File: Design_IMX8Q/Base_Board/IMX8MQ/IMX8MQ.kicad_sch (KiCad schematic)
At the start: 25 parts, among them U1 MIMX8MQ6CVAHZAB, U2 IS43LQ32256A-062BLI, U6 SDINBDG4-8G, U7 MT25QUxxxxxx1xW7, X1 ABLNO, Y1 25MHz, Y2 27MHz

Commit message: Adding color on LPDDR4 memory net
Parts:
- removed C19, C20, C21, C22: 10pF, Capacitor_SMD:C_0402_1005Metric, symbol Device:C_Small
- removed C23, C24, C25, C26, C28, C29, C67, C68: 0.1uF, Capacitor_SMD:C_0402_1005Metric, symbol Device:C_Small
- removed C27, C30: 4.7F, Capacitor_SMD:C_0402_1005Metric, symbol Device:C_Small
- removed R1: 240 1%, Resistor_SMD:R_0201_0603Metric, symbol Device:R_Small
- removed R10, R9: 1M, Resistor_SMD:R_0402_1005Metric, symbol Device:R_Small
- removed R2: 240, Resistor_SMD:R_0402_1005Metric, symbol Device:R_Small
- removed U1: MIMX8MQ6CVAHZAB, IMX8MQ_footprints:MIMX8MQ6CVAHZAB, symbol _MIMX8MQ6CVAHZAB:MIMX8MQ6CVAHZAB
- removed U2: IS43LQ32256A-062BLI, Package_BGA:BGA-200_10.0x14.5mm_Layout12x22_P0.80x0.65mm, symbol Memory_RAM:IS43LQ32256A-062BLI
- removed U6: SDINBDG4-8G, _W_SBC:BGA153C50P14X14_1300X1150X80N, symbol SDINBDG4-8G:SDINBDG4-8G
- removed U7: MT25QUxxxxxx1xW7, Package_DFN_QFN:W-PDFN-8-1EP_6x5mm_P1.27mm_EP3x3mm, symbol Memory_Flash:MT25QUxxxxxx1xW7
- removed X1: ABLNO, Oscillator:Oscillator_SMD_EuroQuartz_XO32-4Pin_3.2x2.5mm_HandSoldering, symbol Oscillator:ABLNO
- removed Y1: 25MHz, Crystal:Crystal_SMD_3225-4Pin_3.2x2.5mm, symbol Device:Crystal_GND24_Small
- removed Y2: 27MHz, Crystal:Crystal_SMD_3225-4Pin_3.2x2.5mm, symbol Device:Crystal_GND24_Small
- added J1: Bus_PCI_Express_x16, Connector_PCBEdge:BUS_PCIexpress_x16, symbol Connector:Bus_PCI_Express_x16
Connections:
- new net: J1.A10 (+3.3V), J1.A9 (+3.3V), J1.B8 (+3.3V)
- new net: J1.A12 (GND), J1.A15 (GND), J1.A18 (GND), J1.A20 (GND), J1.A23 (GND), J1.A24 (GND), J1.A27 (GND), J1.A28 (GND), J1.A31 (GND), J1.A34 (GND), J1.A37 (GND), J1.A38 (GND), J1.A4 (GND), J1.A41 (GND), J1.A42 (GND), J1.A45 (GND), J1.A46 (GND), J1.A49 (GND), J1.A51 (GND), J1.A54 (GND), J1.A55 (GND), J1.A58 (GND), J1.A59 (GND), J1.A62 (GND), J1.A63 (GND), J1.A66 (GND), J1.A67 (GND), J1.A70 (GND), J1.A71 (GND), J1.A74 (GND), J1.A75 (GND), J1.A78 (GND), J1.A79 (GND), J1.A82 (GND), J1.B13 (GND), J1.B16 (GND), J1.B18 (GND), J1.B21 (GND), J1.B22 (GND), J1.B25 (GND), J1.B26 (GND), J1.B29 (GND), J1.B32 (GND), J1.B35 (GND), J1.B36 (GND), J1.B39 (GND), J1.B4 (GND), J1.B40 (GND), J1.B43 (GND), J1.B44 (GND), J1.B47 (GND), J1.B49 (GND), J1.B52 (GND), J1.B53 (GND), J1.B56 (GND), J1.B57 (GND), J1.B60 (GND), J1.B61 (GND), J1.B64 (GND), J1.B65 (GND), J1.B68 (GND), J1.B69 (GND), J1.B7 (GND), J1.B72 (GND), J1.B73 (GND), J1.B76 (GND), J1.B77 (GND), J1.B80 (GND)
- new net: J1.A2 (+12V), J1.A3 (+12V), J1.B1 (+12V), J1.B2 (+12V), J1.B3 (+12V)
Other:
- sheet System Power renamed GND
- added sheet Clock (Clock.kicad_sch)
- added sheet GPIO I2C MIPI ENET HDMI JTAG (GPIO_I2C_MIPI_ENET_HDMI_JTAG.kicad_sch)
- added sheet LPDDR4 (LPDDR4.kicad_sch)
- added sheet NAND MIPI PCIE (NAND_MIPI_PCIE.kicad_sch)
- added sheet Power_IMX8 (Power_IMX8.kicad_sch)
- added sheet SAI SD SPDIF USB UART (SAI-SD-SPDIF-USB-UART.kicad_sch)
- added sheet VDD (PowerSystem.kicad_sch)

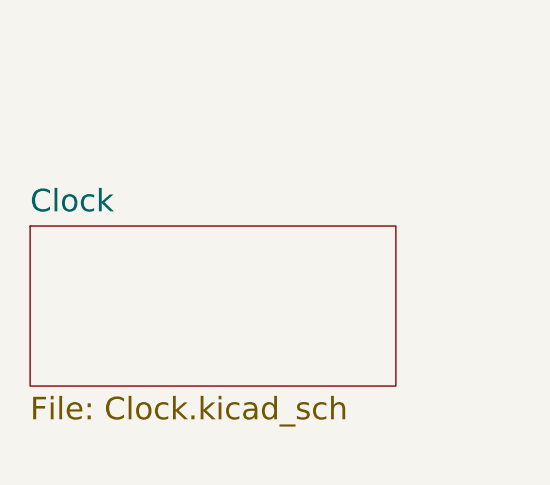
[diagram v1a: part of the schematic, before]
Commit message: changes vias pad size
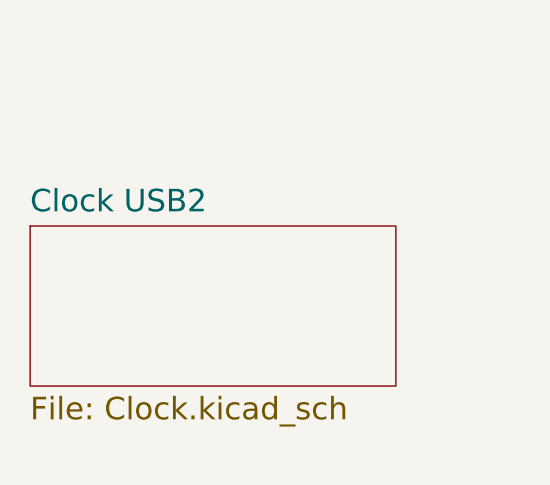
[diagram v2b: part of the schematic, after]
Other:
- sheet Clock renamed Clock USB2
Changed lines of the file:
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@@
     (stroke (width 0.1524) (type solid))
     (fill (color 0 0 0 0.0000))
-    (property "Sheetname" "Clock" (at 31.75 38.0434 0)
+    (property "Sheetname" "Clock USB2" (at 31.75 38.0434 0)
       (effects (font (size 2.5 2.5)) (justify left bottom))
     )

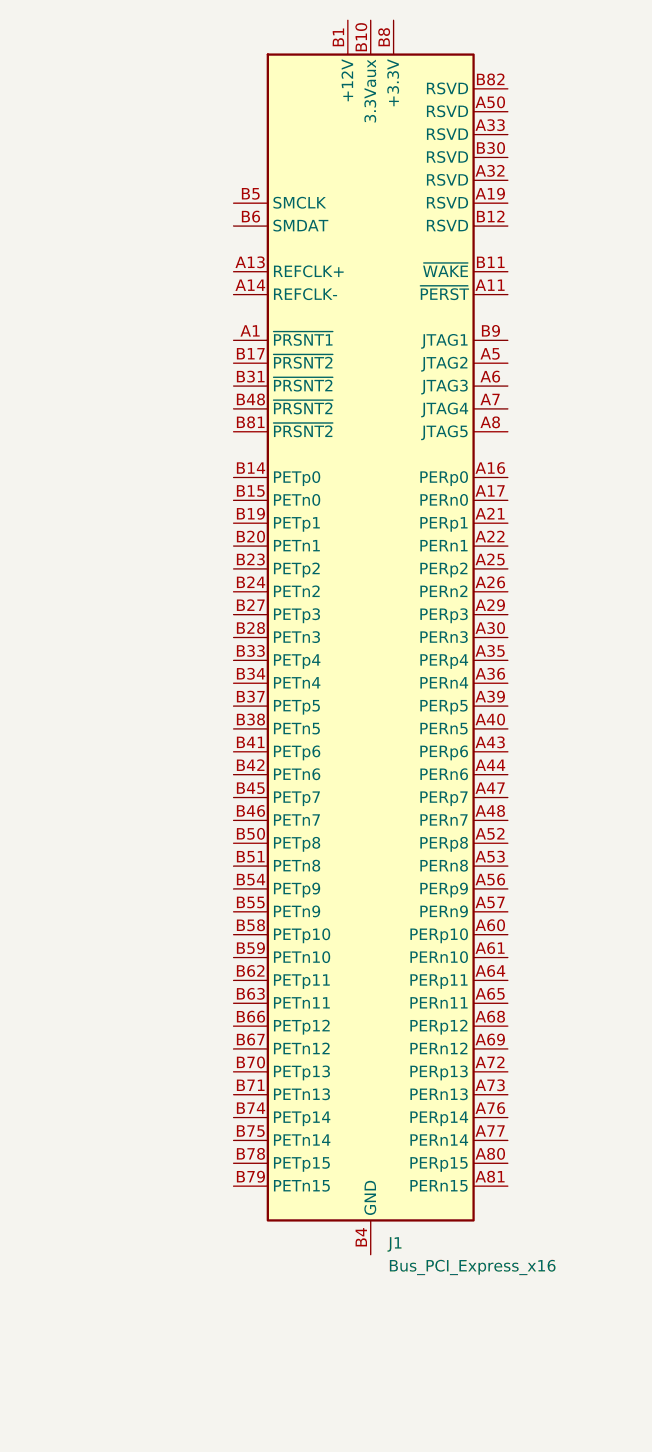
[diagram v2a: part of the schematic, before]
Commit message: Update IMX6QP and IMX8MQ
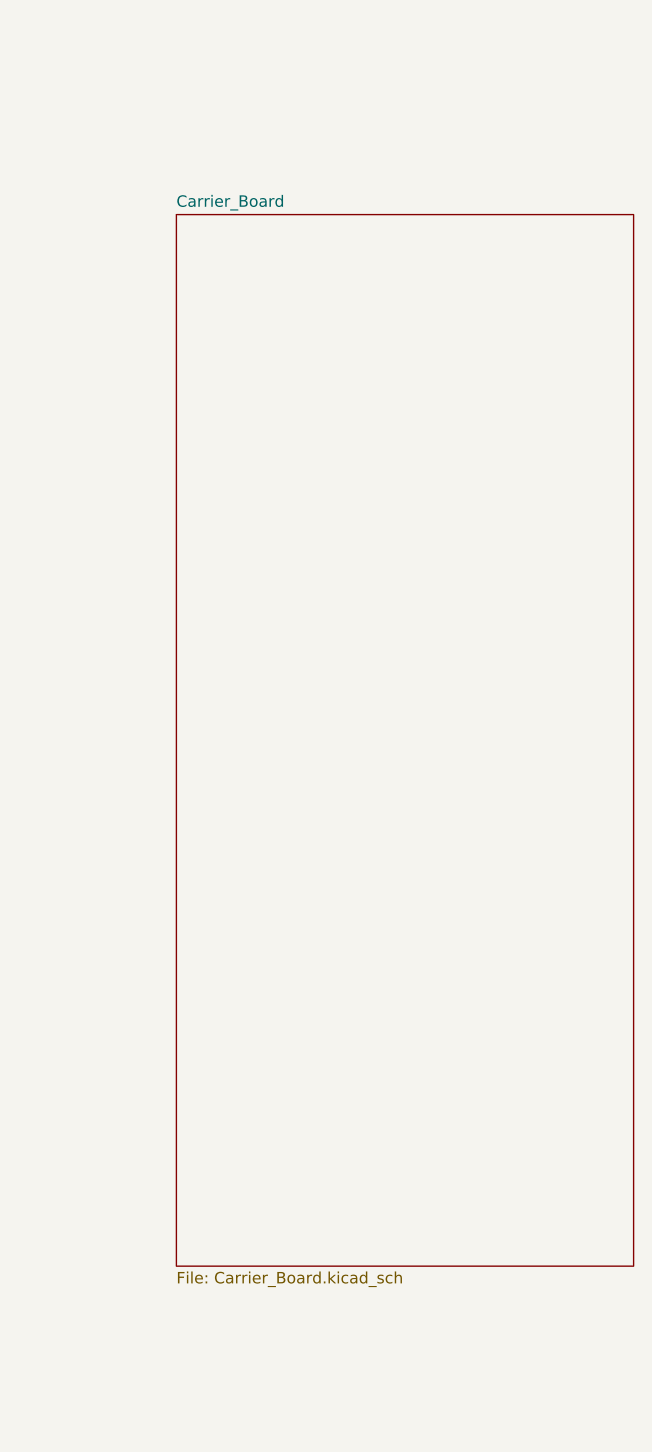
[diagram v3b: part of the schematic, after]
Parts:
- removed J1: Bus_PCI_Express_x16, Connector_PCBEdge:BUS_PCIexpress_x16, symbol Connector:Bus_PCI_Express_x16
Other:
- added sheet Carrier_Board (Carrier_Board.kicad_sch)
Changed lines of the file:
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@@
 (kicad_sch (version 20230121) (generator eeschema)
   (paper "A4")
-  (symbol (lib_id "Connector:Bus_PCI_Express_x16") (at 237.49 85.09 0) (unit 1)
-    (in_bom yes) (on_board yes) (dnp no) (fields_autoplaced)
-    (property "Reference" "J1" (at 239.4459 152.4 0)
-      (effects (font (size 1.27 1.27)) (justify left))
+  (sheet (at 215.9 38.1) (size 50.8 116.84) (fields_autoplaced)
+    (stroke (width 0.1524) (type solid))
+    (fill (color 0 0 0 0.0000))
+    (property "Sheetname" "Carrier_Board" (at 215.9 37.3884 0)
+      (effects (font (size 1.27 1.27)) (justify left bottom))
     )
-    (property "Value" "Bus_PCI_Express_x16" (at 239.4459 154.94 0)
-      (effects (font (size 1.27 1.27)) (justify left))
+    (property "Sheetfile" "Carrier_Board.kicad_sch" (at 215.9 155.5246 0)
+      (effects (font (size 1.27 1.27)) (justify left top))
     )
-    (property "Footprint" "Connector_PCBEdge:BUS_PCIexpress_x16" (at 237.49 62.23 0)
-      (effects (font (size 1.27 1.27)) hide)
-    )
-    (property "Datasheet" "http://www.ritrontek.com/uploadfile/2016/1026/20161026105231124.pdf#page=63" (at 236.22 91.44 0)
-      (effects (font (size 1.27 1.27)) hide)
-    )
-    (pin "A1")
-    (pin "A10")
-    (pin "A11")
-    (pin "A12")
-    (pin "A13")
-    (pin "A14")
-    (pin "A15")
-    (pin "A16")
-    (pin "A17")
-    (pin "A18")
-    (pin "A19")
-    (pin "A2")
-    (pin "A20")
-    (pin "A21")
-    (pin "A22")
-    (pin "A23")
-    (pin "A24")
-    (pin "A25")
-    (pin "A26")
-    (pin "A27")
-    (pin "A28")
-    (pin "A29")
-    (pin "A3")
-    (pin "A30")
-    (pin "A31")
-    (pin "A32")
-    (pin "A33")
-    (pin "A34")
-    (pin "A35")
-    (pin "A36")
-    (pin "A37")
-    (pin "A38")
-    (pin "A39")
-    (pin "A4")
-    (pin "A40")
-    (pin "A41")
-    (pin "A42")
-    (pin "A43")
-    (pin "A44")
-    (pin "A45")
-    (pin "A46")
-    (pin "A47")
-    (pin "A48")
-    (pin "A49")
-    (pin "A5")
-    (pin "A50")
-    (pin "A51")
-    (pin "A52")
-    (pin "A53")
-    (pin "A54")
-    (pin "A55")
-    (pin "A56")
-    (pin "A57")
-    (pin "A58")
-    (pin "A59")
-    (pin "A6")
-    (pin "A60")
-    (pin "A61")
-    (pin "A62")
-    (pin "A63")
-    (pin "A64")
-    (pin "A65")
-    (pin "A66")
-    (pin "A67")
-    (pin "A68")
-    (pin "A69")
-    (pin "A7")
-    (pin "A70")
-    (pin "A71")
-    (pin "A72")
-    (pin "A73")
-    (pin "A74")
-    (pin "A75")
-    (pin "A76")
-    (pin "A77")
-    (pin "A78")
-    (pin "A79")
-    (pin "A8")
-    (pin "A80")
-    (pin "A81")
-    (pin "A82")
-    (pin "A9")
-    (pin "B1")
-    (pin "B10")
-    (pin "B11")
-    (pin "B12")
-    (pin "B13")
-    (pin "B14")
-    (pin "B15")
-    (pin "B16")
-    (pin "B17")
-    (pin "B18")
-    (pin "B19")
-    (pin "B2")
-    (pin "B20")
-    (pin "B21")
-    (pin "B22")
-    (pin "B23")
-    (pin "B24")
-    (pin "B25")
-    (pin "B26")
-    (pin "B27")
-    (pin "B28")
-    (pin "B29")
-    (pin "B3")
-    (pin "B30")
-    (pin "B31")
-    (pin "B32")
-    (pin "B33")
-    (pin "B34")
-    (pin "B35")
-    (pin "B36")
-    (pin "B37")
-    (pin "B38")
-    (pin "B39")
-    (pin "B4")
-    (pin "B40")
-    (pin "B41")
-    (pin "B42")
-    (pin "B43")
-    (pin "B44")
-    (pin "B45")
-    (pin "B46")
-    (pin "B47")
-    (pin "B48")
-    (pin "B49")
-    (pin "B5")
-    (pin "B50")
-    (pin "B51")
-    (pin "B52")
-    (pin "B53")
-    (pin "B54")
-    (pin "B55")
-    (pin "B56")
-    (pin "B57")
-    (pin "B58")
-    (pin "B59")
-    (pin "B6")
-    (pin "B60")
-    (pin "B61")
-    (pin "B62")
-    (pin "B63")
-    (pin "B64")
-    (pin "B65")
-    (pin "B66")
-    (pin "B67")
-    (pin "B68")
-    (pin "B69")
-    (pin "B7")
-    (pin "B70")
-    (pin "B71")
-    (pin "B72")
-    (pin "B73")
-    (pin "B74")
-    (pin "B75")
-    (pin "B76")
-    (pin "B77")
-    (pin "B78")
-    (pin "B79")
-    (pin "B8")
-    (pin "B80")
-    (pin "B81")
-    (pin "B82")
-    (pin "B9")
     (instances
       (project "IMX8MQ"
-        (path "/980bb0ed-9dcc-491b-96e4-a3efce564505"
-          (reference "J1") (unit 1)
-        )
+        (path "/980bb0ed-9dcc-491b-96e4-a3efce564505" (page "10"))
       )
     )
